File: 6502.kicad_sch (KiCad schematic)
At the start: 34 parts, among them J3 Conn_01x40, J4 CPU Control, SW1 Reset, U1 W65C02SxP, U2 AT28C256, U3 HM62256BLP, Y1 1MHz

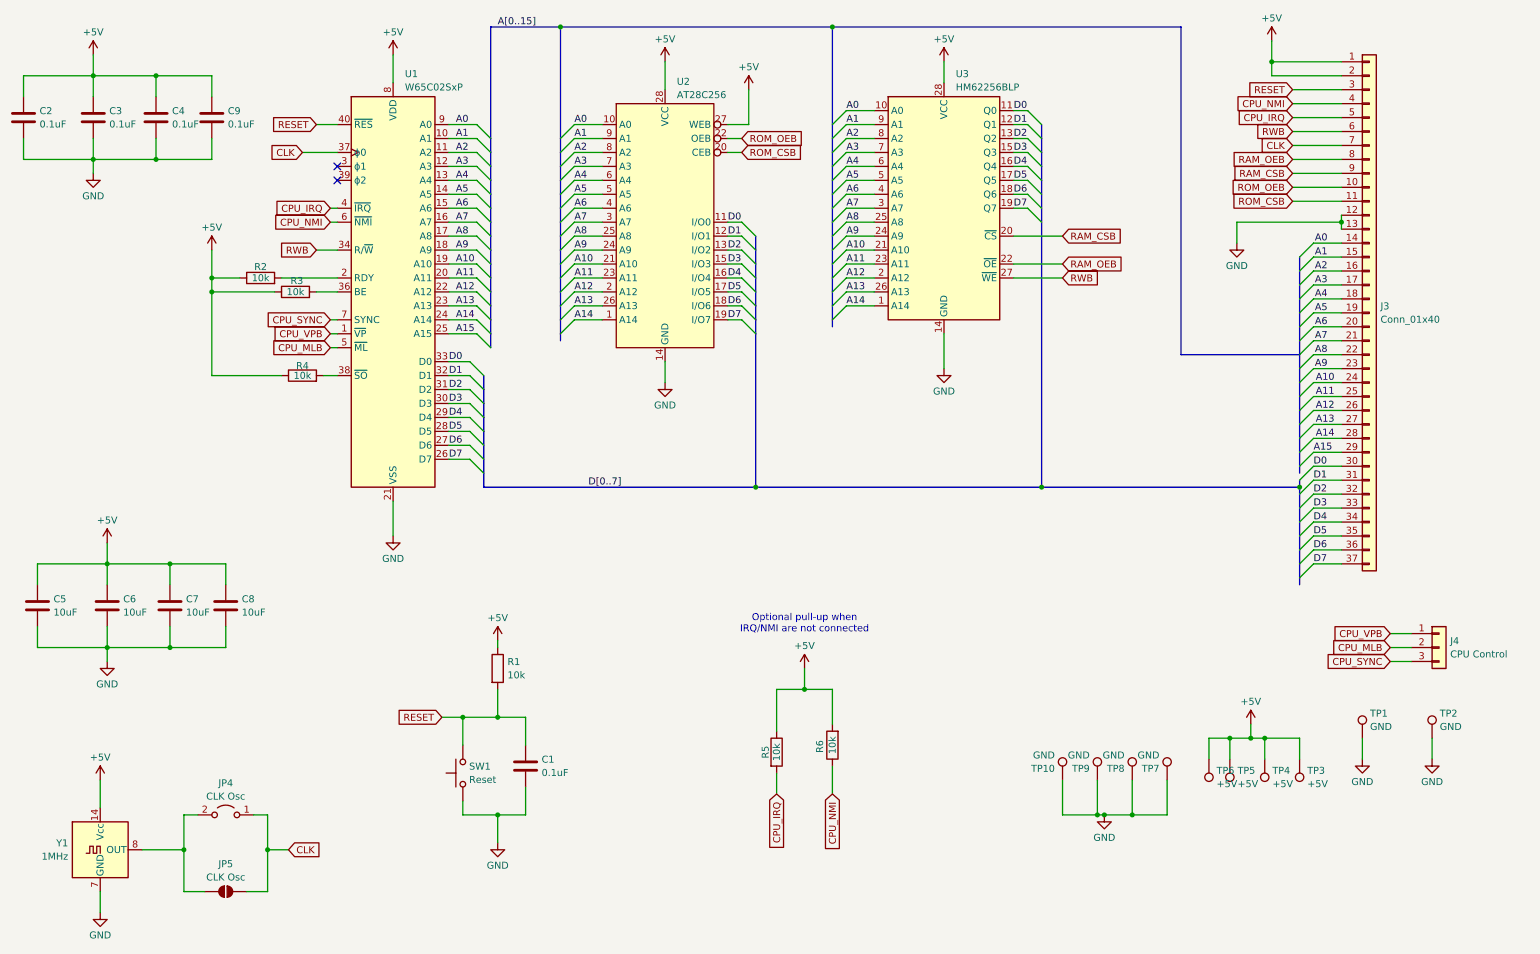
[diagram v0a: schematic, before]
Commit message: Replace back-plane connector
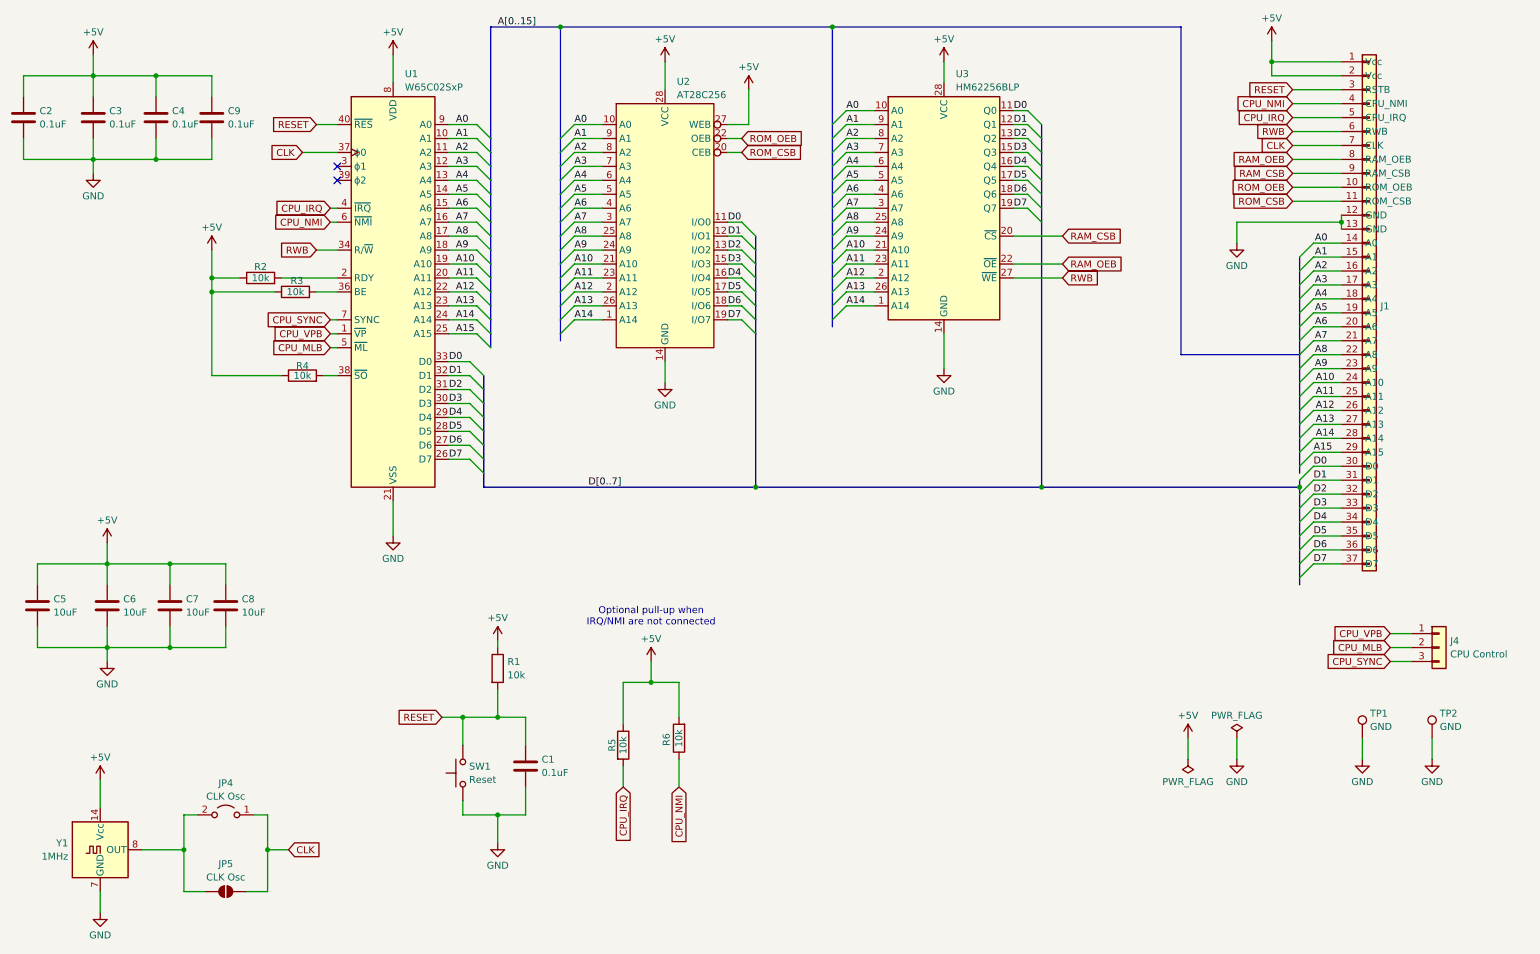
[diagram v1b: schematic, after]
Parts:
- removed J3: Conn_01x40, Connector_PinHeader_2.54mm:PinHeader_1x37_P2.54mm_Vertical, symbol Connector_Generic:Conn_01x37
- removed TP10, TP7, TP8, TP9: GND, TestPoint:TestPoint_Pad_D1.5mm, symbol Connector:TestPoint
- removed TP3, TP4, TP5, TP6: +5V, TestPoint:TestPoint_Pad_D1.5mm, symbol Connector:TestPoint
- added J1: ~, Connector_PinHeader_2.54mm:PinHeader_1x37_P2.54mm_Vertical, symbol backplane:Connector
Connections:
- net +5V: now also J1.1 (Vcc), J1.2 (Vcc)
- net A0: now also J1.14 (A0)
- net A1: now also J1.15 (A1)
- net A10: now also J1.24 (A10)
- net A11: now also J1.25 (A11)
- net A12: now also J1.26 (A12)
- net A13: now also J1.27 (A13)
- net A14: now also J1.28 (A14)
- net A15: now also J1.29 (A15)
- net A2: now also J1.16 (A2)
- net A3: now also J1.17 (A3)
- net A4: now also J1.18 (A4)
- net A5: now also J1.19 (A5)
- net A6: now also J1.20 (A6)
- net A7: now also J1.21 (A7)
- net A8: now also J1.22 (A8)
- net A9: now also J1.23 (A9)
- net CLK: now also J1.7 (CLK)
- net CPU_IRQ: now also J1.5 (CPU_IRQ)
- net CPU_NMI: now also J1.4 (CPU_NMI)
- net D0: now also J1.30 (D0)
- net D1: now also J1.31 (D1)
- net D2: now also J1.32 (D2)
- net D3: now also J1.33 (D3)
- net D4: now also J1.34 (D4)
- net D5: now also J1.35 (D5)
- net D6: now also J1.36 (D6)
- net D7: now also J1.37 (D7)
- net GND: now also J1.12 (GND), J1.13 (GND)
- net RAM_CSB: now also J1.9 (RAM_CSB)
- net RAM_OEB: now also J1.8 (RAM_OEB)
- net RESET: now also J1.3 (RSTB)
- net ROM_CSB: now also J1.11 (ROM_CSB)
- net ROM_OEB: now also J1.10 (ROM_OEB)
- net RWB: now also J1.6 (RWB)
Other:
- moved on the sheet: R5, R6

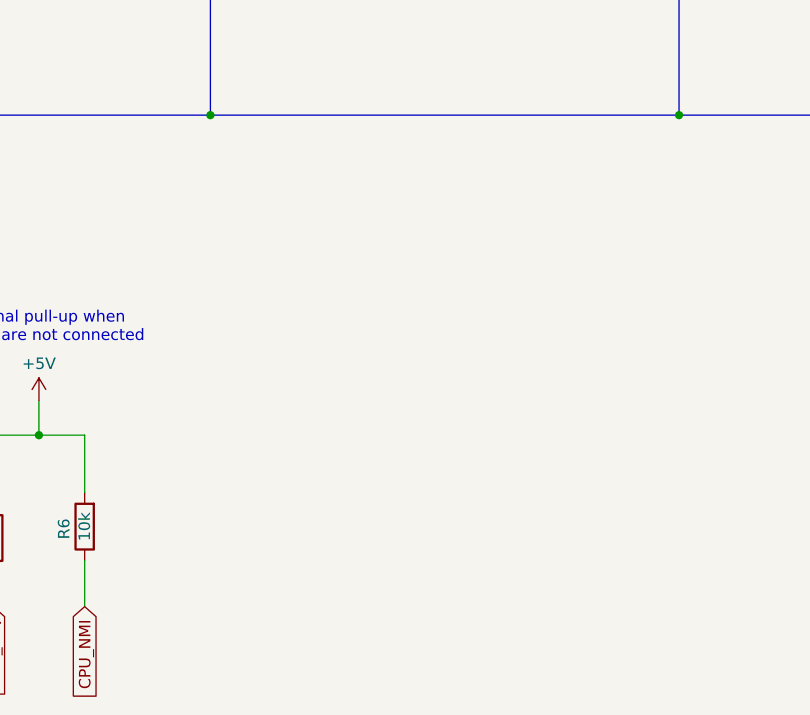
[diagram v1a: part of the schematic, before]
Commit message: Status LEDs
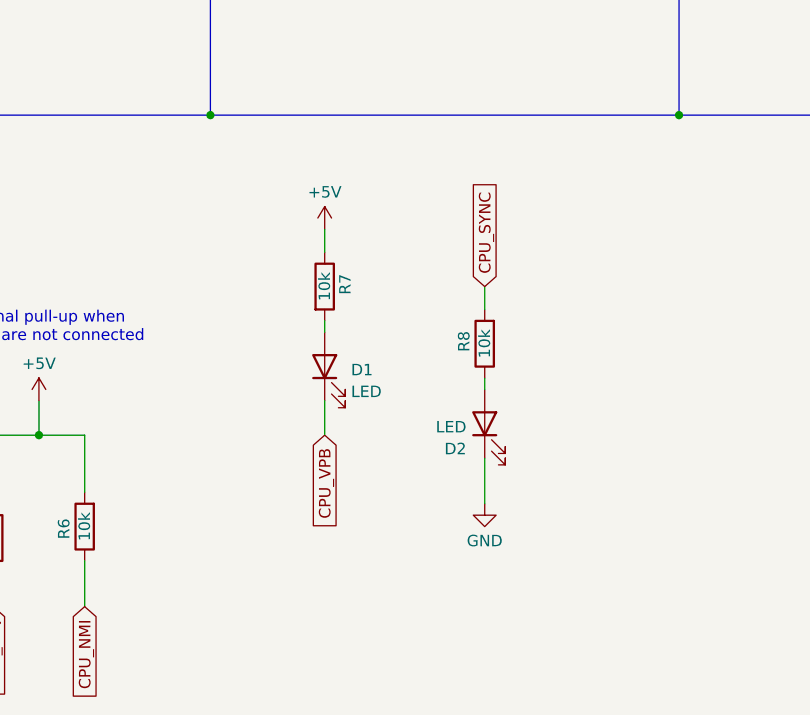
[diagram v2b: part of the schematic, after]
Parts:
- added D1, D2: LED, LED_THT:LED_D3.0mm_Horizontal_O1.27mm_Z2.0mm, symbol Device:LED
- added R7, R8: 10k, Resistor_SMD:R_1206_3216Metric, symbol Device:R
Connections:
- net +5V: now also R7.1
- net CPU_SYNC: now also R8.2
- net CPU_VPB: now also D1.1 (K)
- net GND: now also D2.1 (K)
- new net: D1.2 (A), R7.2
- new net: D2.2 (A), R8.1
